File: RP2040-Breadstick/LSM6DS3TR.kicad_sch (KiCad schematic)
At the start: 3 parts, among them U401 LSM6DSMTR

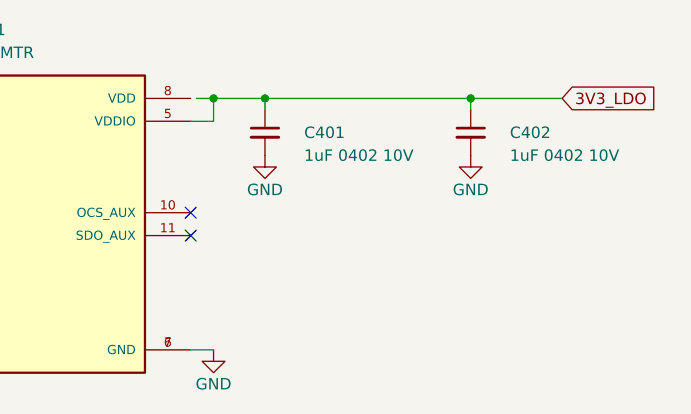
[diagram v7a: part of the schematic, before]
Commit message: Placed uC caps, flash, and ADC
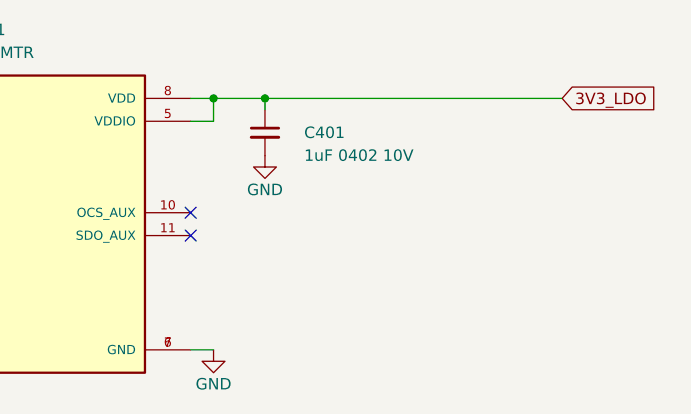
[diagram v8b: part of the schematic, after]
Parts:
- removed C402: 1uF 0402 10V, _Breadstick_Footprints:Perfect_0402_Cap, symbol Device:C_Small
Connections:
- net 3V3_LDO: now also U401.8 (VDD)
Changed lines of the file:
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@@
     (comment 4 "https://github.com/mrangen/RP2040-Breadstick")
-  )
-  (junction (at 203.2 81.28) (diameter 0) (color 0 0 0 0)
   )
   (junction (at 174.625 81.28) (diameter 0) (color 0 0 0 0)
@@
     (stroke (width 0) (type default) (color 0 0 0 0))
   )
-  (wire (pts (xy 203.2 81.28) (xy 213.36 81.28))
-    (stroke (width 0) (type default) (color 0 0 0 0))
-  )
   (wire (pts (xy 126.365 96.52) (xy 126.365 97.79))
     (stroke (width 0) (type default) (color 0 0 0 0))
@@
     (stroke (width 0) (type default) (color 0 0 0 0))
   )
-  (wire (pts (xy 180.34 81.28) (xy 203.2 81.28))
+  (wire (pts (xy 180.34 81.28) (xy 213.36 81.28))
     (stroke (width 0) (type default) (color 0 0 0 0))
   )
@@
     (stroke (width 0) (type default) (color 0 0 0 0))
   )
-  (wire (pts (xy 203.2 81.28) (xy 203.2 82.55))
-    (stroke (width 0) (type default) (color 0 0 0 0))
-  )
-  (wire (pts (xy 172.72 81.28) (xy 174.625 81.28))
+  (wire (pts (xy 172.085 81.28) (xy 174.625 81.28))
     (stroke (width 0) (type default) (color 0 0 0 0))
   )
@@
     (pin "2")
   )
-  (symbol (lib_id "power:GND") (at 203.2 87.63 0) (unit 1)
-    (in_bom yes) (on_board yes)
-    (property "Reference" "#PWR0404" (id 0) (at 203.2 93.98 0)
-      (effects (font (size 1.27 1.27)) hide)
-    )
-    (property "Value" "GND" (id 1) (at 203.2 91.44 0))
-    (property "Footprint" "" (id 2) (at 203.2 87.63 0)
-      (effects (font (size 1.27 1.27)) hide)
-    )
-    (property "Datasheet" "" (id 3) (at 203.2 87.63 0)
-      (effects (font (size 1.27 1.27)) hide)
-    )
-    (pin "1")
-  )
   (symbol (lib_id "power:GND") (at 180.34 87.63 0) (unit 1)
     (in_bom yes) (on_board yes)
@@
     (pin "1")
   )
-  (symbol (lib_id "Device:C_Small") (at 203.2 85.09 0) (mirror y) (unit 1)
-    (in_bom yes) (on_board yes)
-    (property "Reference" "C402" (id 0) (at 212.09 85.09 0)
-      (effects (font (size 1.27 1.27)) (justify left))
-    )
-    (property "Value" "1uF 0402 10V" (id 1) (at 219.71 87.63 0)
-      (effects (font (size 1.27 1.27)) (justify left))
-    )
-    (property "Footprint" "_Breadstick_Footprints:Perfect_0402_Cap" (id 2) (at 203.2 85.09 0)
-      (effects (font (size 1.27 1.27)) hide)
-    )
-    (property "Datasheet" "~" (id 3) (at 203.2 85.09 0)
-      (effects (font (size 1.27 1.27)) hide)
-    )
-    (property "JLCPCB P/N" "" (id 4) (at 203.2 85.09 0)
-      (effects (font (size 1.27 1.27)) hide)
-    )
-    (property "Digikey" "1276-1076-6-ND" (id 5) (at 203.2 85.09 0)
-      (effects (font (size 1.27 1.27)) hide)
-    )
-    (pin "1")
-    (pin "2")
-  )
   (symbol (lib_id "power:GND") (at 174.625 109.22 0) (unit 1)
